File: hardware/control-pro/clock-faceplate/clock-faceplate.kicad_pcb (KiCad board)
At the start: 2 copper layers, 180 x 90 mm, 19 parts

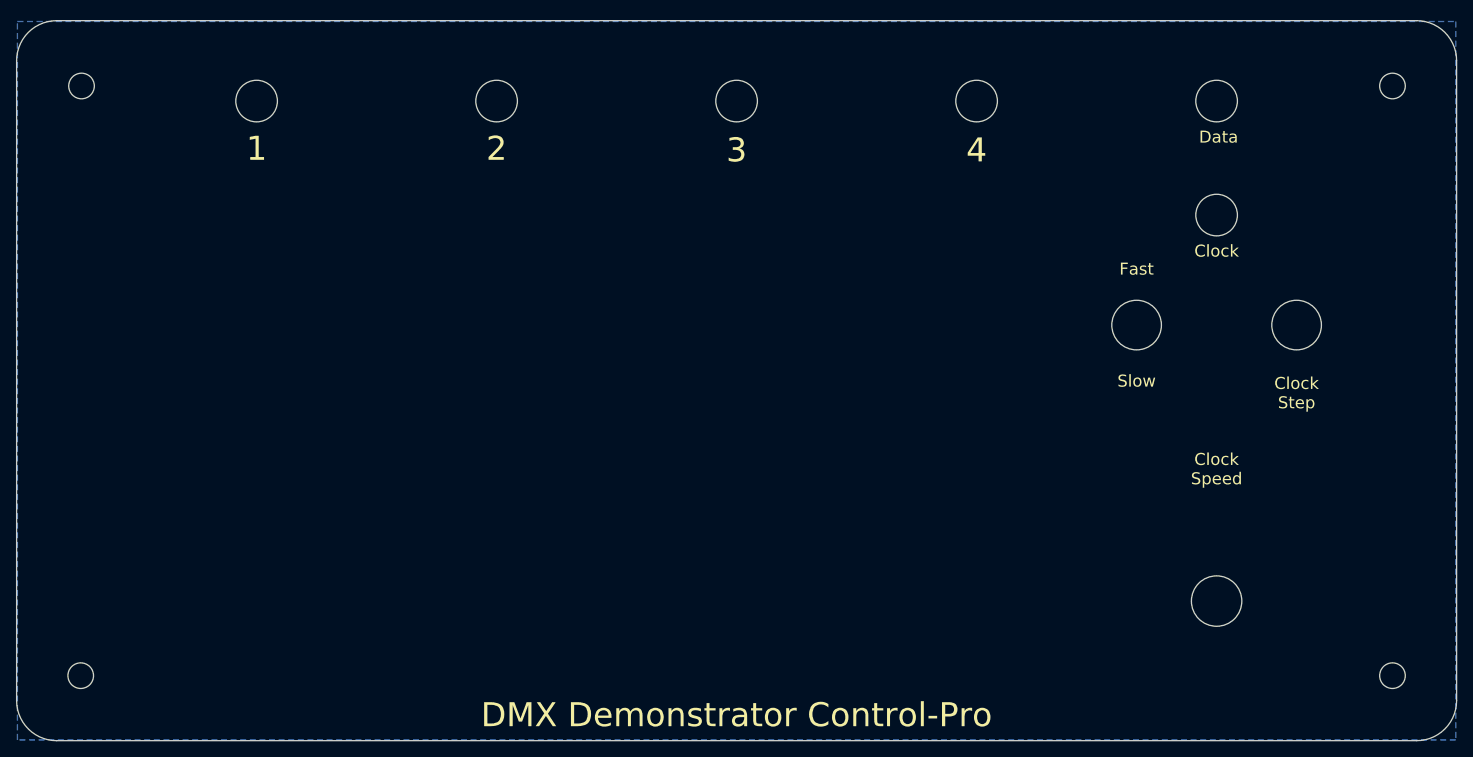
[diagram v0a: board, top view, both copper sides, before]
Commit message: Refactor Control-Pro: - Rename all dimmers to dim1-4 (instead of dim0-3) - Split control-pro into 2 smaller board to save on board cost - clock-control/faceplate only has clock controls - dimmer-control/faceplate only has dimmer controls - both control-pro boards have 2 ribbon cable connectors
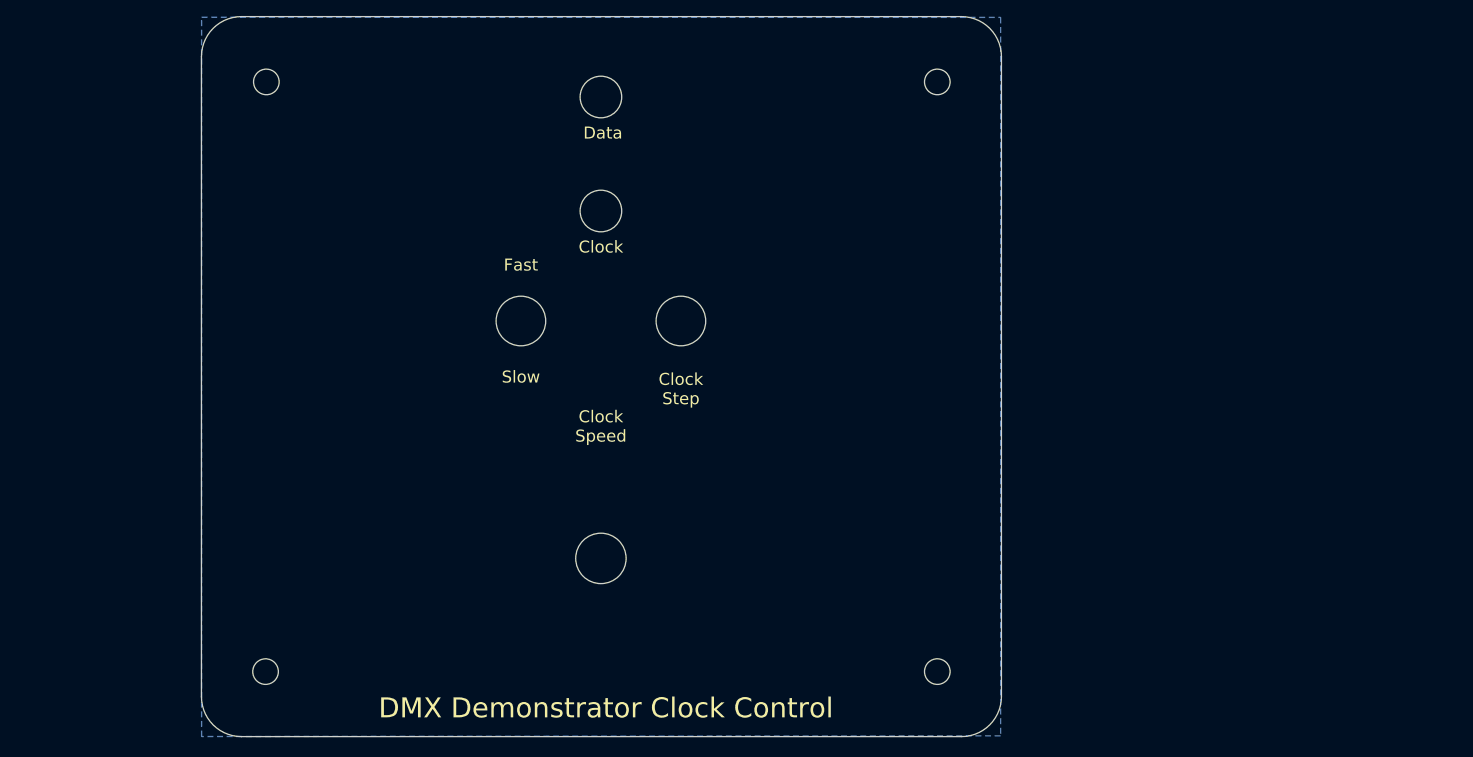
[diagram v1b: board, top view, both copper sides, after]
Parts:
- removed MH11, MH12, MH13, MH14, MH5, MH6, MH7, MH8: MountingHole, MountingHole:MountingHole_3.2mm_M3
- moved G*** 103.7 mm to (149.7, 134.9), turned to 180 degrees
- moved ? 101.7 mm to (171.7, 135.9), turned to 180 degrees
- moved MH17 77.1 mm to (137.0, 116.4)
- moved MH15 77.0 mm to (127.0, 86.7)
- moved MH10 77.0 mm to (137.0, 73.0)
- moved MH16 77.0 mm to (147.0, 86.7)
- moved MH9 77.0 mm to (137.0, 58.7)
- moved MH3 56.9 mm to (179.1, 56.9)
- moved MH4 56.9 mm to (179.1, 130.6)
- moved MH1 23.1 mm to (95.2, 56.9)
- moved MH2 23.1 mm to (95.1, 130.6)
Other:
- board size 180 x 90 mm -> 100 x 90 mm
- board text added: "DMX Demonstrator Clock Control"
- board text added: "DMX-CPCF, Rev 1.2 Crazy Giraffe Software"
- board text removed: "1"
- board text removed: "2"
- board text removed: "3"
- board text removed: "4"
- board text removed: "DMX Demonstrator Control-Pro"
- board text removed: "DMX-CPF, Rev 1.1 Crazy Giraffe Software"

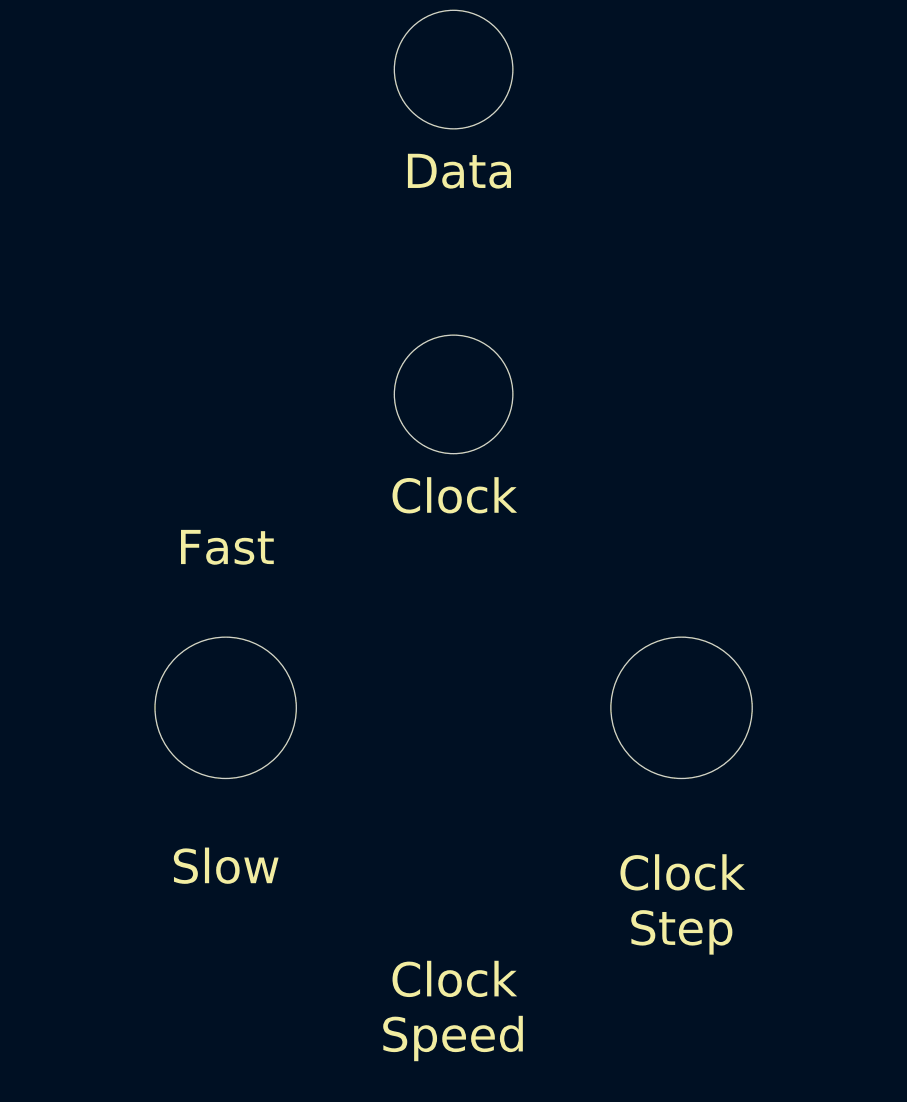
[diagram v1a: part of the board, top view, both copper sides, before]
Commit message: TX2: - Added buffer to drive LEDs - Added decoupling capacitors - Fixed dimmer traces on PCB
DMX-CPC*:
- Switched to horizontal 16 pin connectors since vertical was too tall with a cable plugged in
- Swapped the clock speed and step switches to match the order on the TX1
- Swapped the data and clock LEDs to match the order on the TX1

DMX-CPD*:
- Split dimmer controls out to its own PCB
- Added 2nd 16 pin connector to daisy chain with DMX-CPC*.
- Switched to horizontal 16 pin connectors since vertical was too tall with a cable plugged in

Updated readmes with parts, board links.
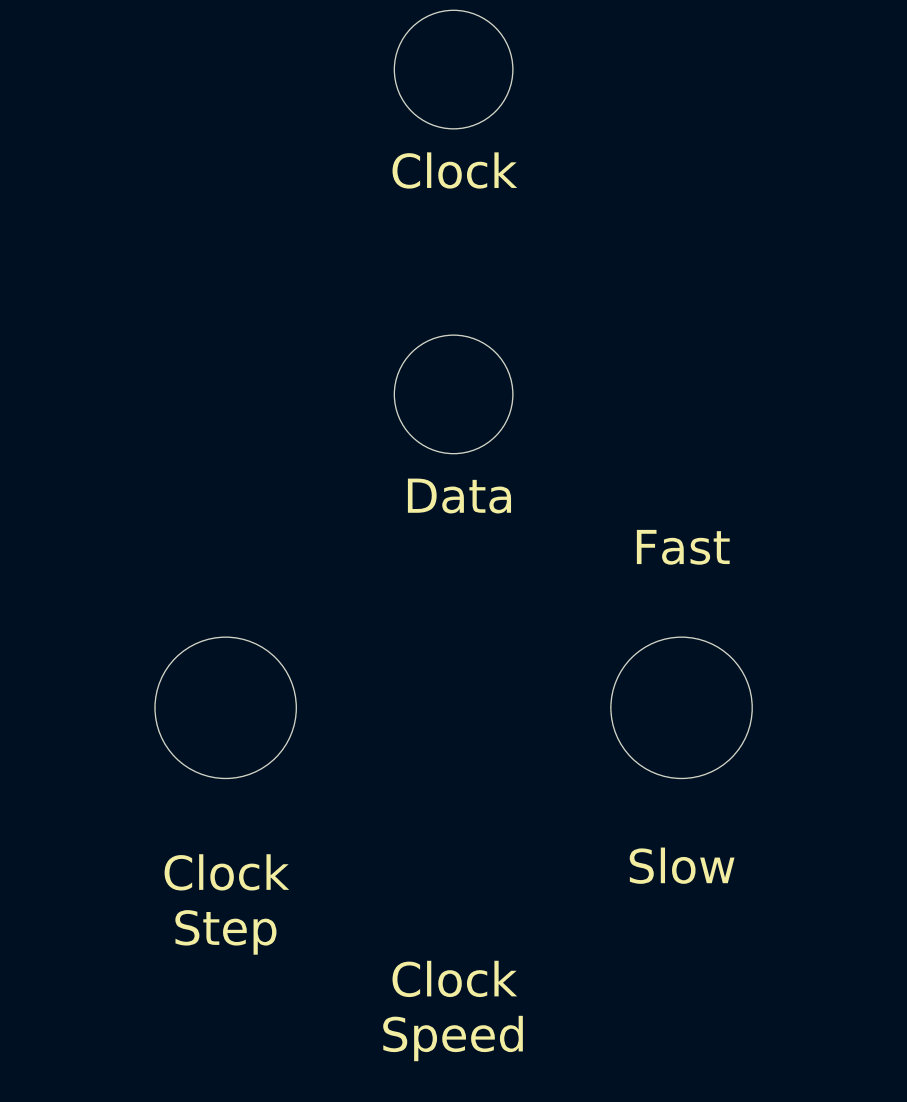
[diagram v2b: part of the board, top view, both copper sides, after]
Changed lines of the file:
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@@
   (title_block
     (title "DMX Demonstrator - Control-Pro Clock (DMX-CPCF)")
-    (date 2022-09-06)
+    (date 2023-02-11)
     (rev 1.2)
     (company "Crazy Giraffe Software")
@@
     (effects (font (size 1.5 1.5) (thickness 0.3)))
   )
-  (gr_text Data (at 137.288 63.242) (layer F.SilkS)
+  (gr_text Data (at 137.288 77.492) (layer F.SilkS)
     (effects (font (size 1.5 1.5) (thickness 0.3)))
   )
-  (gr_text Clock (at 137.038 77.492) (layer F.SilkS)
+  (gr_text Clock (at 137.038 63.242) (layer F.SilkS)
     (effects (font (size 1.5 1.5) (thickness 0.3)))
   )
@@
     (effects (font (size 1 1) (thickness 0.15)) (justify mirror))
   )
-  (gr_text Fast (at 127.038 79.742) (layer F.SilkS)
+  (gr_text Fast (at 147.038 79.742) (layer F.SilkS)
     (effects (font (size 1.5 1.5) (thickness 0.3)))
   )
-  (gr_text Slow (at 127.038 93.742) (layer F.SilkS)
+  (gr_text Slow (at 147.038 93.742) (layer F.SilkS)
     (effects (font (size 1.5 1.5) (thickness 0.3)))
   )
@@
   (gr_line (start 92.184 49.092) (end 92.184 138.492) (layer Dwgs.User) (width 0.1524))
   (gr_line (start 87.304 93.692) (end 186.904 93.692) (layer Dwgs.User) (width 0.1524))
-  (gr_text "Clock\nStep" (at 147.038 95.242) (layer F.SilkS)
+  (gr_text "Clock\nStep" (at 127.038 95.242) (layer F.SilkS)
     (effects (font (size 1.5 1.5) (thickness 0.3)))
   )
